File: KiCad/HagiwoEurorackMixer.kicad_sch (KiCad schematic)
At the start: 22 parts, among them J1 AudioJack2_SwitchT, J2 AudioJack2_SwitchT, J3 AudioJack2_SwitchT, J4 AudioJack2_SwitchT, J5 AudioJack2_SwitchT, J6 EURO_PWR_2x5, U2 TL072

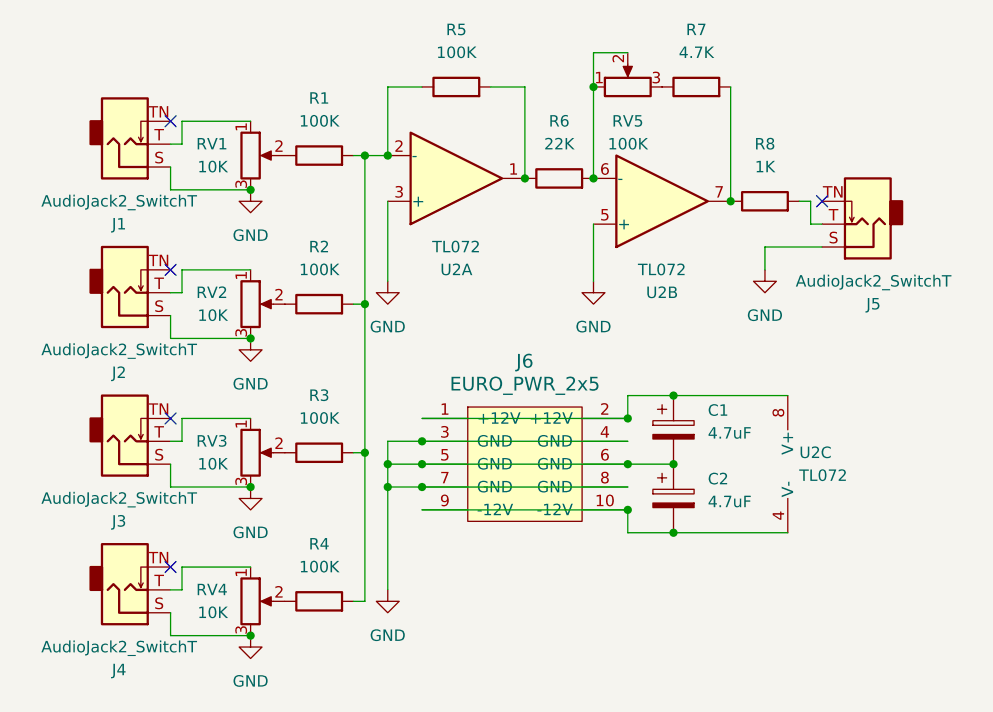
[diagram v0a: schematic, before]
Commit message: v1.1 complete - fixed power header orientation, implemented ground plane, equal horizontal spacing from board edge for pots and jacks, flipped some components to back and reoriented, rerouted, redesigned panel
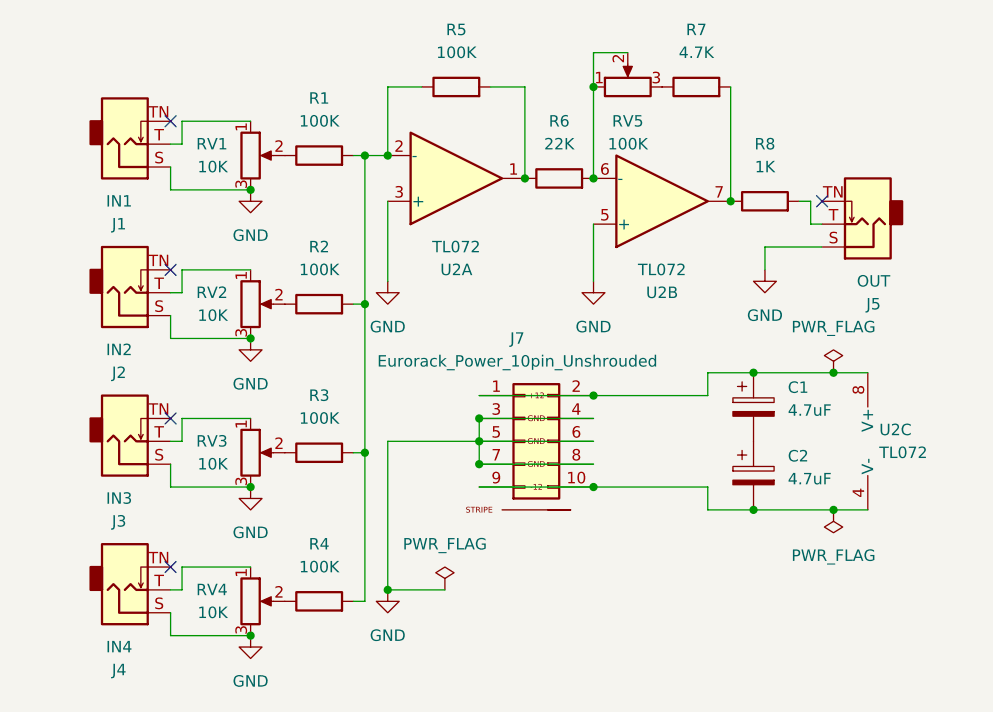
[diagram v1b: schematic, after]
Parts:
- removed J6: EURO_PWR_2x5, Connector_IDC:IDC-Header_2x05_P2.54mm_Vertical, symbol eurocad:EURO_PWR_2x5
- added J7: Eurorack_Power_10pin_Unshrouded, Library:IDC-Header_2x05_P2.54mm_Vertical_Euro_Power_Striped, symbol PCM_4ms_Connector:Eurorack_Power_10pin_Unshrouded
- J1: value AudioJack2_SwitchT -> IN1; footprint eurocad:PJ301M-12_T_S -> Library:EighthInch_PJ398SM_T_TN_S
- J2: value AudioJack2_SwitchT -> IN2; footprint eurocad:PJ301M-12_T_S -> Library:EighthInch_PJ398SM_T_TN_S
- J3: value AudioJack2_SwitchT -> IN3; footprint eurocad:PJ301M-12_T_S -> Library:EighthInch_PJ398SM_T_TN_S
- J4: value AudioJack2_SwitchT -> IN4; footprint eurocad:PJ301M-12_T_S -> Library:EighthInch_PJ398SM_T_TN_S
- J5: value AudioJack2_SwitchT -> OUT; footprint eurocad:PJ301M-12_T_S -> Library:EighthInch_PJ398SM_T_TN_S
- RV1, RV2, RV3, RV4: footprint eurocad:Alpha9mmPot -> Library:Pot_9mm_DShaft_RemovedPins4_5
- RV5: footprint eurocad:Alpha9mmPot -> LibraryAll:Pot_9mm_DShaft_RemovedPins4_5
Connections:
- net GND: now also J7.3 (GND), J7.4 (GND), J7.5 (GND), J7.6 (GND), J7.7 (GND), J7.8 (GND); no longer C1.2, C2.1
- net at C1.1, U2.8 (V+): now also J7.1 (+12V), J7.2 (+12V)
- net at C2.2, U2.4 (V-): now also J7.10 (-12V), J7.9 (-12V)
- new net: C1.2, C2.1
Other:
- title: (none) -> Hagiwo Eurorack Mixer
- moved on the sheet: C1, C2, U2C
